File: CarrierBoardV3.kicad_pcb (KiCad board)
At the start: 4 copper layers, 92 x 96 mm, 86 parts, among them J1 USB_B_Micro, J10 Conn_02x26_Odd_Even, J2 Conn_02x09_Odd_Even, J3 Barrel_Jack, J4 TX2iConnctor, J5 Conn_01x03_Male, J6 Conn_02x04_Odd_Even, J7 Conn_02x03_Odd_Even, J8 Conn_02x26_Odd_Even, J9 Conn_01x03_Male, SW1 SW_Push, SW2 SW_Push, SW3 SW_Push, U1 MAX3221, U2 FT232RQ, U3 MSATA-Socket, U4 TXB0104PW, U5 TXB0104PW, U6 MPM3620, U7 LP38851LINREG, U8 MPM3620

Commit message: Layout clean ups and revisions
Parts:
- moved U4 10.4 mm to (130.5, 94.7)
- moved U5 10.2 mm to (130.6, 103.2)
- moved J6 1.28 mm to (105.4, 64.5)
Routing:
- net Net-(U1-Pad13): track 19.1 -> 64.7 mm
- net Net-(U1-Pad8): track 28.5 -> 64.7 mm
- net I2C_DAT: track 16.8 -> 39.6 mm, vias 0 -> 2
- net GBE_LINK1000#: track 75.3 -> 52.5 mm
- net I2C_GP1_DAT: track 69.1 -> 52.5 mm
- net SPI0_MOSI: track 79.2 -> 62.9 mm
- net I2C_GP1_CK: track 68.8 -> 52.7 mm
- net GBE_MDI2+: track 86.0 -> 71.3 mm
- net SATA_RX-: track 27.7 -> 13.2 mm
- net GBE_MDI3+: track 88.0 -> 75.4 mm
- net SPI0_CS0#: track 76.0 -> 63.5 mm
- net UART0_RX: track 77.6 -> 89.6 mm, vias 1 -> 3
- net GBE_MDI1-: track 67.3 -> 55.4 mm
- net SATA_RX+: track 25.7 -> 13.8 mm
- net SPI0_MISO: track 83.2 -> 71.5 mm
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
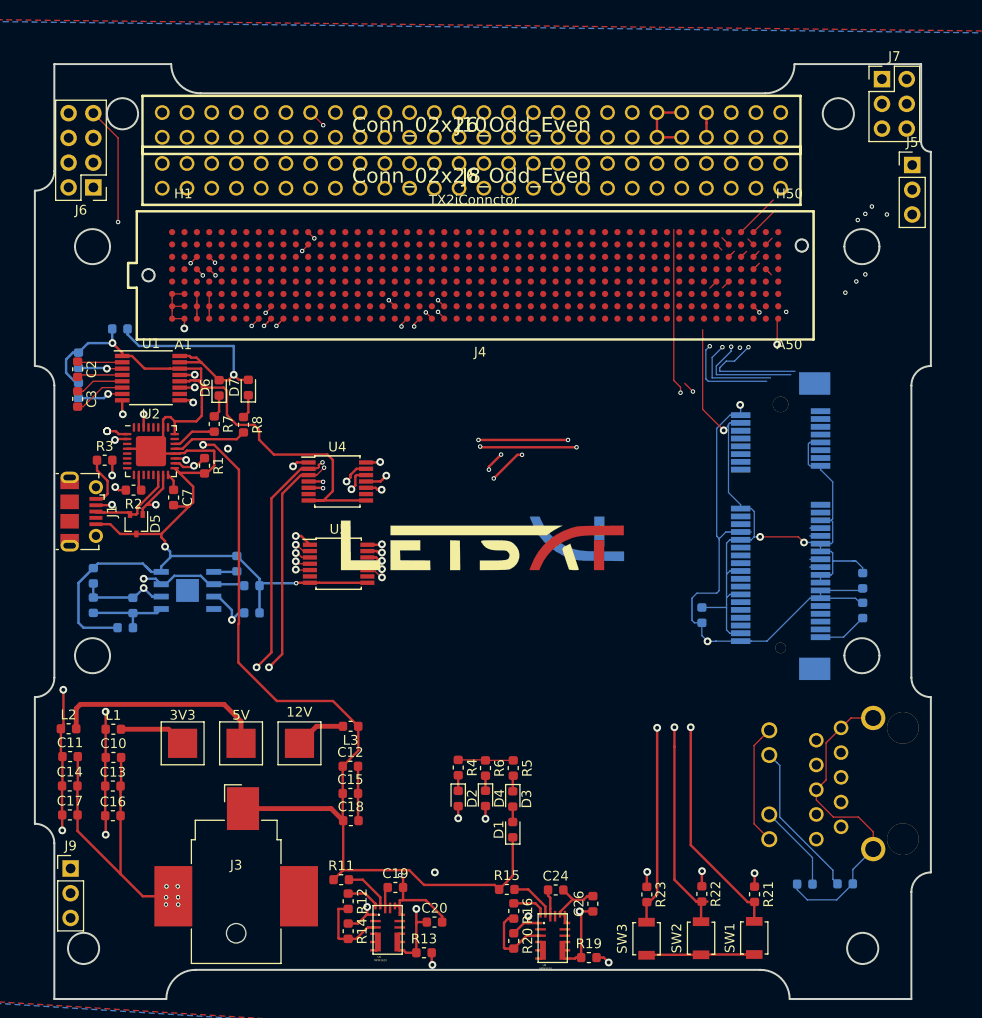
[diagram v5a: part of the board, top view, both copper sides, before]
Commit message: Layout revisions for signal and power lines
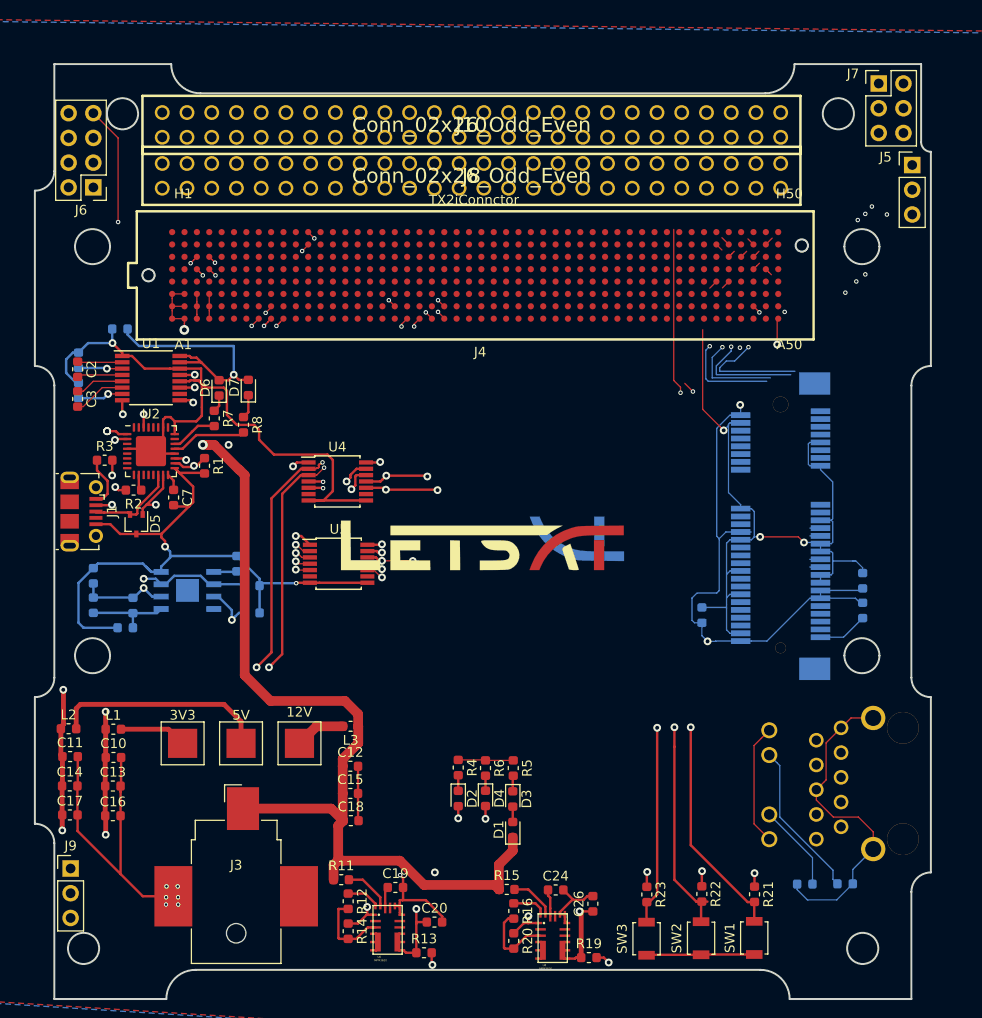
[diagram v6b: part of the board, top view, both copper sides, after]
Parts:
- moved R7 0.58 mm to (117.8, 88.2)
- moved J7 0.56 mm to (186.1, 53.9)
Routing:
- net I2C_GP1_CK: track 52.7 -> 86.9 mm, vias 3 -> 2
- net SPI0_MOSI: track 62.9 -> 93.3 mm, vias 1 -> 2
- net SPI0_CS0#: track 63.5 -> 93.1 mm, vias 3 -> 1
- net I2C_GP1_DAT: track 52.5 -> 79.4 mm, vias 3 -> 2
- net SPI0_CLK: track 66.4 -> 93.1 mm, vias 3 -> 1
- net SPI0_MISO: track 71.5 -> 94.0 mm
- net GBE_CTREF(GND): track 346.3 -> 337.7 mm, vias 14 -> 13
- net BCR_OUT: track 7.62 -> 0.00 mm
- net TX2i_3V3: track 244.9 -> 251.0 mm
- net GBE_MDI3+: track 75.4 -> 70.7 mm
- net GBE_MDI3-: track 83.2 -> 80.0 mm
- net TX2i_VBATT: track 2.54 -> 0.00 mm
- net TX2i_12V: track 112.1 -> 114.6 mm
- net Net-(D6-Pad1): track 2.34 -> 1.77 mm

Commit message: ethernet trace matches finished
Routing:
- net GBE_LINK1000#: track 52.5 -> 99.4 mm, vias 1 -> 3
- net GBE_MDI0-: track 52.9 -> 96.1 mm
- net GBE_MDI0+: track 49.7 -> 87.0 mm
- net GBE_MDI1-: track 55.4 -> 87.0 mm
- net SATA_TX-: track 11.6 -> 41.6 mm, vias 1 -> 4
- net SATA_TX+: track 11.9 -> 41.7 mm, vias 1 -> 4
- net SATA_RX+: track 13.8 -> 41.5 mm, vias 1 -> 4
- net SATA_RX-: track 13.2 -> 40.8 mm, vias 1 -> 4
- net GBE_MDI1+: track 63.5 -> 87.0 mm, vias 1 -> 3
- net GBE_MDI3+: track 70.7 -> 87.0 mm
- net GBE_MDI2+: track 71.3 -> 87.0 mm
- net GBE_MDI2-: track 75.2 -> 87.0 mm
- net GBE_CTREF(GND): track 337.7 -> 326.9 mm
- net GBE_MDI3-: track 80.0 -> 87.0 mm
- net PWRBTNn: track 78.8 -> 75.2 mm
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
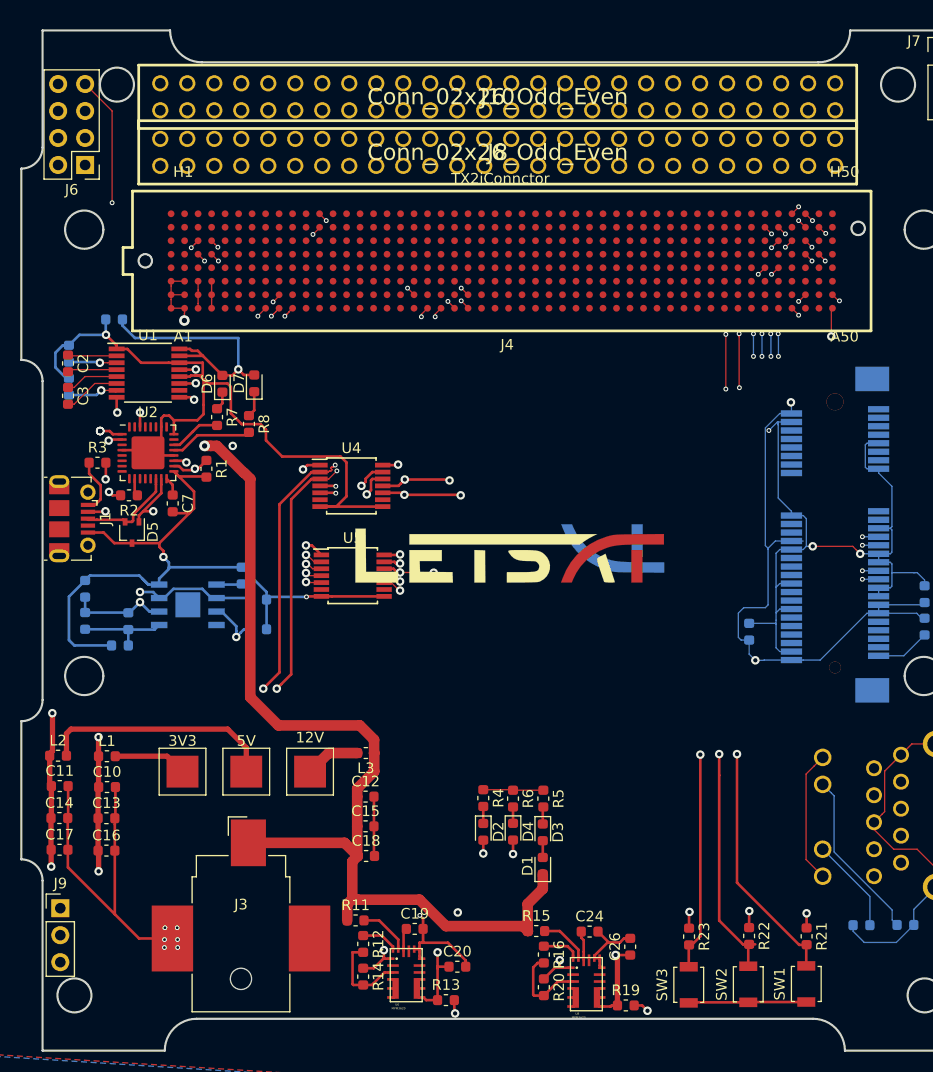
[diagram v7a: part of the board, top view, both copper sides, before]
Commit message: done with all trace revisions, need to add sata connector holes and verify with prabodh on a DRC problem, all routes are connected
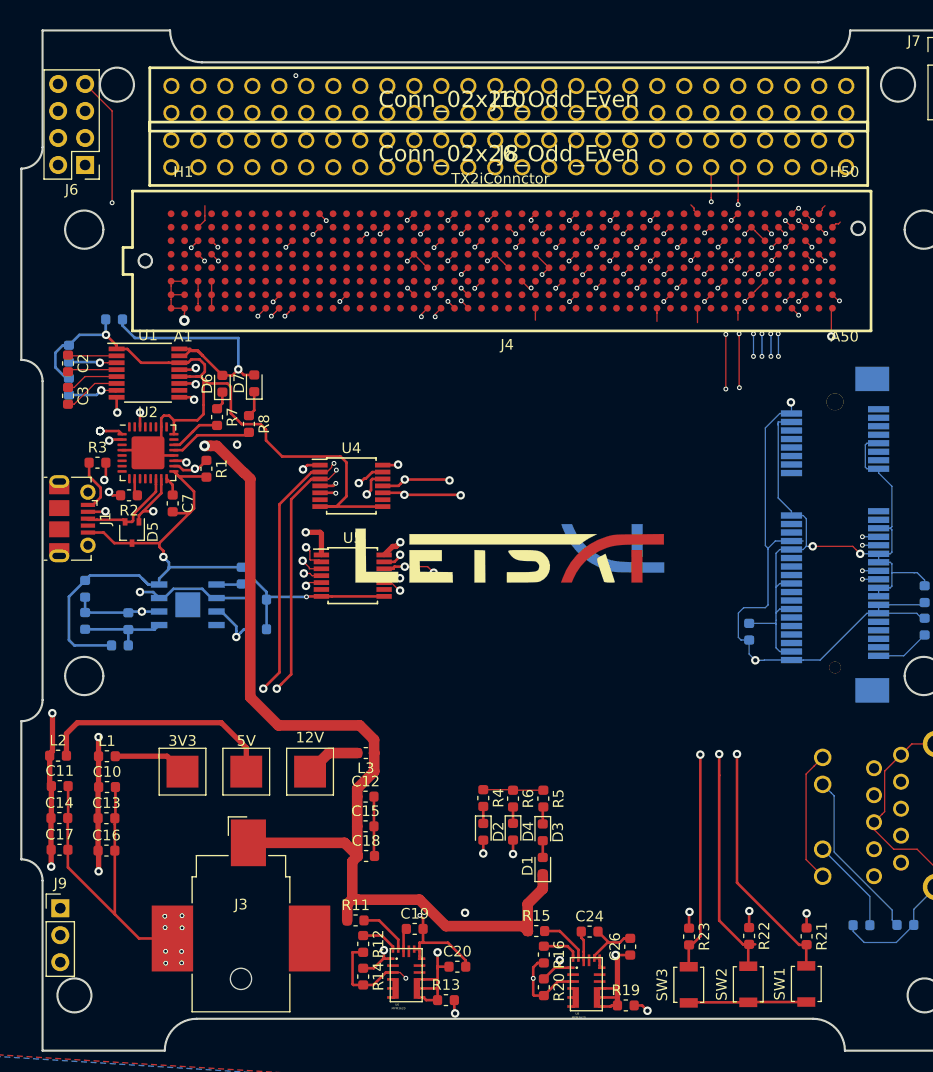
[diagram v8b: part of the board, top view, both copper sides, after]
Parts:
- moved J10 1.08 mm to (145.3, 58.4)
- moved J8 1.04 mm to (145.3, 63.5)
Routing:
- net GBE_CTREF(GND): track 326.9 -> 405.9 mm, vias 13 -> 74
- net TX2i_3V3: track 251.0 -> 323.7 mm
- net TX2i_5V: track 240.9 -> 307.0 mm
- net TX2i_12V: track 114.6 -> 149.8 mm
- net GNDA: track 16.5 -> 29.8 mm, vias 0 -> 2
- net BCR_OUT: track 0.00 -> 7.62 mm
- net I2C_GP1_CK: track 86.9 -> 90.6 mm, vias 2 -> 3
- net I2C_GP1_DAT: track 79.4 -> 82.8 mm, vias 2 -> 3
- net TX2i_VBATT: track 0.00 -> 2.54 mm
- net PCM_IN: track 0.00 -> 2.54 mm
- net TX2i_1.8V: track 43.6 -> 44.3 mm
